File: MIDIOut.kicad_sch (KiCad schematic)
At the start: 6 parts, among them J201 SJ2-25504B-SMT-TR, U201 74AHC1G125

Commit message: Udpate
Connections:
- net Tip: now also J201.2 (T)
- no-connect marks 3 -> 2
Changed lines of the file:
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@@
 	(title_block
 		(title "MIDI Out")
-		(date "2024-01-03")
-		(rev "1")
+		(date "2024-03-12")
+		(rev "2")
+	)
+	(junction
+		(at 180.34 109.22)
+		(diameter 0)
+		(color 0 0 0 0)
 	)
 	(junction
@@
 		(at 182.88 104.14)
 	)
-	(no_connect
-		(at 182.88 114.3)
+	(wire
+		(pts
+			(xy 180.34 109.22) (xy 182.88 109.22)
+		)
+		(stroke
+			(width 0)
+			(type default)
+		)
 	)
 	(wire
@@
 	(wire
 		(pts
+			(xy 180.34 114.3) (xy 180.34 109.22)
+		)
+		(stroke
+			(width 0)
+			(type default)
+		)
+	)
+	(wire
+		(pts
 			(xy 97.79 109.22) (xy 97.79 116.84)
 		)
@@
 	(wire
 		(pts
-			(xy 144.78 109.22) (xy 182.88 109.22)
+			(xy 144.78 109.22) (xy 180.34 109.22)
+		)
+		(stroke
+			(width 0)
+			(type default)
+		)
+	)
+	(wire
+		(pts
+			(xy 182.88 114.3) (xy 180.34 114.3)
 		)
 		(stroke
@@
 		(at 198.12 107.95 0)
 		(unit 1)
-		(exclude_from_sim yes)
+		(exclude_from_sim no)
 		(in_bom yes)
 		(on_board yes)
@@
 			(at 198.12 107.95 0)
 			(effects
+				(font
+					(size 1.27 1.27)
+				)
+				(hide yes)
+			)
+		)
+		(property "Sim.Enable" "0"
+			(at 198.12 107.95 0)
+			(effects

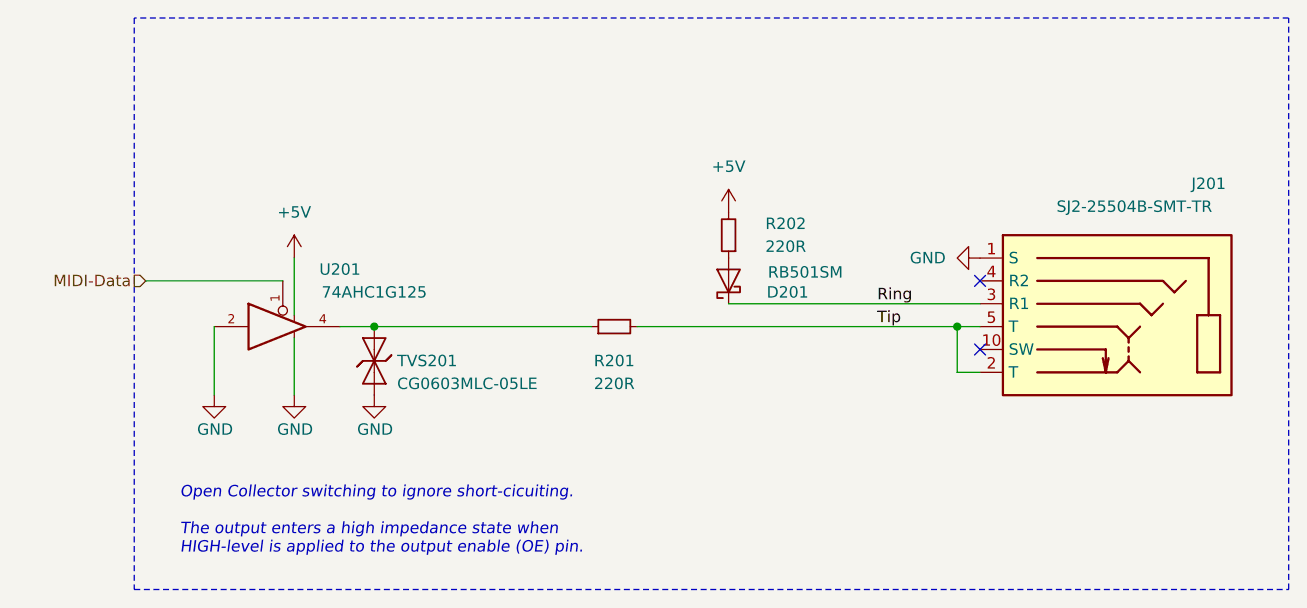
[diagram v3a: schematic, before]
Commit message: Replace TRS sockets
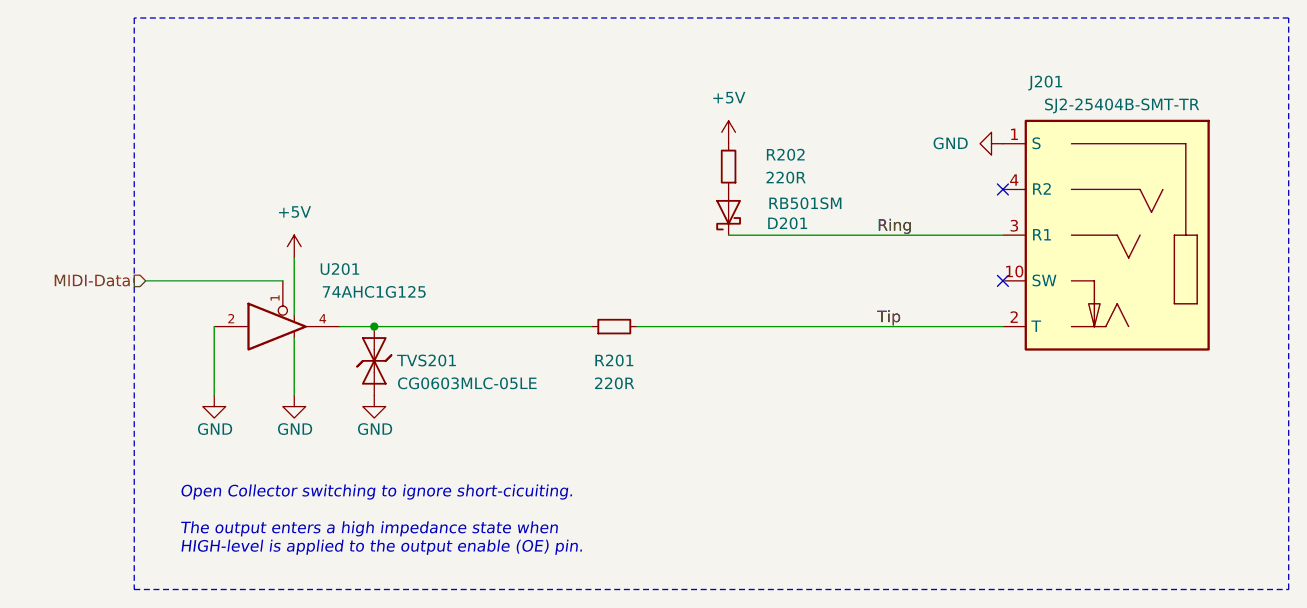
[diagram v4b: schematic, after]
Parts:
- J201: value SJ2-25504B-SMT-TR -> SJ2-25404B-SMT-TR; footprint V2_Connector_Audio:CUI_SJ2-25504B-SMT-TR -> V2_Connector_Audio:CUI_SJ2-25404B-SMT-TR; symbol V2_Connector_Audio:SJ2-25504B-SMT-TR -> V2_Connector_Audio:SJ2-25404B-SMT-TR
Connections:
- net Tip: no longer J201.5 (T)
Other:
- moved on the sheet: D201, R202
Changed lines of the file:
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@@
 	(title_block
 		(title "MIDI Out")
-		(date "2024-03-12")
-		(rev "2")
-	)
-	(junction
-		(at 180.34 109.22)
-		(diameter 0)
-		(color 0 0 0 0)
+		(date "2024-07-17")
+		(rev "3")
 	)
 	(junction
@@
 	)
 	(no_connect
-		(at 182.88 111.76)
+		(at 185.42 104.14)
 	)
 	(no_connect
-		(at 182.88 104.14)
+		(at 185.42 93.98)
 	)
 	(wire
 		(pts
-			(xy 180.34 109.22) (xy 182.88 109.22)
+			(xy 144.78 109.22) (xy 185.42 109.22)
 		)
 		(stroke
@@
 	(wire
 		(pts
-			(xy 154.94 106.68) (xy 182.88 106.68)
+			(xy 154.94 99.06) (xy 185.42 99.06)
 		)
 		(stroke
@@
 	(wire
 		(pts
-			(xy 180.34 114.3) (xy 180.34 109.22)
+			(xy 97.79 109.22) (xy 97.79 116.84)
 		)
 		(stroke
@@
 	(wire
 		(pts
-			(xy 97.79 109.22) (xy 97.79 116.84)
+			(xy 106.68 110.49) (xy 106.68 116.84)
 		)
 		(stroke
@@
 	(wire
 		(pts
-			(xy 106.68 110.49) (xy 106.68 116.84)
-		)
-		(stroke
-			(width 0)
-			(type default)
-		)
-	)
-	(wire
-		(pts
 			(xy 106.68 101.6) (xy 106.68 107.95)
-		)
-		(stroke
-			(width 0)
-			(type default)
-		)
-	)
-	(wire
-		(pts
-			(xy 144.78 109.22) (xy 180.34 109.22)
-		)
-		(stroke
-			(width 0)
-			(type default)
-		)
-	)
-	(wire
-		(pts
-			(xy 182.88 114.3) (xy 180.34 114.3)
 		)
 		(stroke
@@
 	)
 	(label "Ring"
-		(at 171.45 106.68 0)
+		(at 171.45 99.06 0)
 		(fields_autoplaced yes)
 		(effects
@@
 	(symbol
 		(lib_id "Device:R_Small")
-		(at 154.94 99.06 180)
+		(at 154.94 91.44 180)
 		(unit 1)
 		(exclude_from_sim no)
@@
 		(dnp no)
 		(property "Reference" "R202"
-			(at 161.29 97.79 0)
+			(at 161.29 90.17 0)
 			(effects
 				(font
@@
 		)
 		(property "Value" "220R"
-			(at 161.29 100.33 0)
+			(at 161.29 92.71 0)
 			(effects
 				(font
@@
 		)
 		(property "Footprint" "Resistor_SMD:R_0603_1608Metric"
-			(at 154.94 99.06 0)
+			(at 154.94 91.44 0)
 			(effects
 				(font
@@
 		)
 		(property "Datasheet" "~"
-			(at 154.94 99.06 0)
+			(at 154.94 91.44 0)
 			(effects
 				(font
@@
 		)
 		(property "Description" "Resistor, small symbol"
-			(at 154.94 99.06 0)
+			(at 154.94 91.44 0)
 			(effects
 				(font
@@
 	(symbol
 		(lib_id "power:GND")
-		(at 182.88 101.6 270)
+		(at 185.42 88.9 270)
 		(unit 1)
 		(exclude_from_sim no)
@@
 		(fields_autoplaced yes)
 		(property "Reference" "#PWR0202"
-			(at 176.53 101.6 0)
+			(at 179.07 88.9 0)
 			(effects
 				(font
@@
 		)
 		(property "Value" "GND"
-			(at 179.07 101.6 90)
+			(at 181.61 88.9 90)
 			(effects
 				(font
@@
 		)
 		(property "Footprint" ""
-			(at 182.88 101.6 0)
+			(at 185.42 88.9 0)
 			(effects
 				(font
@@
 		)
 		(property "Datasheet" ""
-			(at 182.88 101.6 0)
+			(at 185.42 88.9 0)
 			(effects
 				(font
@@
 		)
 		(property "Description" "Power symbol creates a global label with name \"GND\" , ground"
-			(at 182.88 101.6 0)
+			(at 185.42 88.9 0)
 			(effects
 				(font
@@
 	(symbol
 		(lib_id "V2_Diode:RB501SM")
-		(at 154.94 104.14 90)
+		(at 154.94 96.52 90)
 		(unit 1)
 		(exclude_from_sim no)
@@
 		(dnp no)
 		(property "Reference" "D201"
-			(at 163.83 105.41 90)
+			(at 163.83 97.79 90)
 			(effects
 				(font
@@
 		)
 		(property "Value" "RB501SM"
-			(at 167.64 103.1876 90)
+			(at 167.64 95.5676 90)
 			(effects
 				(font
@@
 		)
 		(property "Footprint" "Diode_SMD:D_SOD-523"
-			(at 161.925 104.14 0)
+			(at 161.925 96.52 0)
 			(effects
 				(font
@@
 		)
 		(property "Datasheet" ""
-			(at 154.94 104.14 0)
+			(at 154.94 96.52 0)
 			(effects
 				(font
@@
 		)
 		(property "Description" ""
-			(at 154.94 104.14 0)
+			(at 154.94 96.52 0)
 			(effects
 				(font
@@
 	)
 	(symbol
-		(lib_id "V2_Connector_Audio:SJ2-25504B-SMT-TR")
-		(at 198.12 107.95 0)
-		(unit 1)
-		(exclude_from_sim yes)
+		(lib_id "V2_Connector_Audio:SJ2-25404B-SMT-TR")
+		(at 198.12 99.06 0)
+		(mirror y)
+		(unit 1)
+		(exclude_from_sim no)
 		(in_bom yes)
 		(on_board yes)
 		(dnp no)
 		(property "Reference" "J201"
-			(at 208.28 93.345 0)
-			(effects
-				(font
-					(size 1.27 1.27)
-				)
-			)
-		)
-		(property "Value" "SJ2-25504B-SMT-TR"
-			(at 200.025 95.885 0)
-			(effects
-				(font
-					(size 1.27 1.27)
-				)
-			)
-		)
-		(property "Footprint" "V2_Connector_Audio:CUI_SJ2-25504B-SMT-TR"
-			(at 173.99 123.19 0)
+			(at 190.246 82.042 0)
+			(effects
+				(font
+					(size 1.27 1.27)
+				)
+			)
+		)
+		(property "Value" "SJ2-25404B-SMT-TR"
+			(at 198.628 84.582 0)
+			(effects
+				(font
+					(size 1.27 1.27)
+				)
+			)
+		)
+		(property "Footprint" "V2_Connector_Audio:CUI_SJ2-25404B-SMT-TR"
+			(at 210.312 119.634 0)
 			(effects
 				(font
@@
 		)
 		(property "Datasheet" ""
-			(at 198.12 107.95 0)
+			(at 198.12 99.06 0)
 			(effects
 				(font
@@
 		)
 		(property "Description" ""
-			(at 198.12 107.95 0)
-			(effects
-				(font
-					(size 1.27 1.27)
-				)
-				(hide yes)
-			)
-		)
-		(property "Sim.Enable" "0"
-			(at 198.12 107.95 0)
-			(effects
-				(font
-					(size 1.27 1.27)
-				)
+			(at 206.248 122.174 0)
+			(effects
+				(font
+					(size 1.27 1.27)
+				)
+				(justify left bottom)
 				(hide yes)
 			)
@@
 		(pin "4"
 		)
-		(pin "5"
-		)
 		(instances
 			(project "express"
@@
 	(symbol
 		(lib_id "power:+5V")
-		(at 154.94 96.52 0)
+		(at 154.94 88.9 0)
 		(unit 1)
 		(exclude_from_sim no)
@@
 		(fields_autoplaced yes)
 		(property "Reference" "#PWR0207"
-			(at 154.94 100.33 0)
+			(at 154.94 92.71 0)
 			(effects
 				(font
@@
 		)
 		(property "Value" "+5V"
-			(at 154.94 91.44 0)
+			(at 154.94 83.82 0)
 			(effects
 				(font
@@
 		)
 		(property "Footprint" ""
-			(at 154.94 96.52 0)
+			(at 154.94 88.9 0)
 			(effects
 				(font
@@
 		)
 		(property "Datasheet" ""
-			(at 154.94 96.52 0)
+			(at 154.94 88.9 0)
 			(effects
 				(font
@@
 		)
 		(property "Description" "Power symbol creates a global label with name \"+5V\""
-			(at 154.94 96.52 0)
-			(effects
-				(font
+			(at 154.94 88.9 0)
+			(effects
+				(font
